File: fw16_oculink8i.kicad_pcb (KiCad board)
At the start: 4 copper layers, 118.7 x 72.5 mm, 24 parts, among them J1 FXBeam, J2 Fan0, J3 Fan1, J4 173162-0131, U1 BR24G32FVT-3GE2

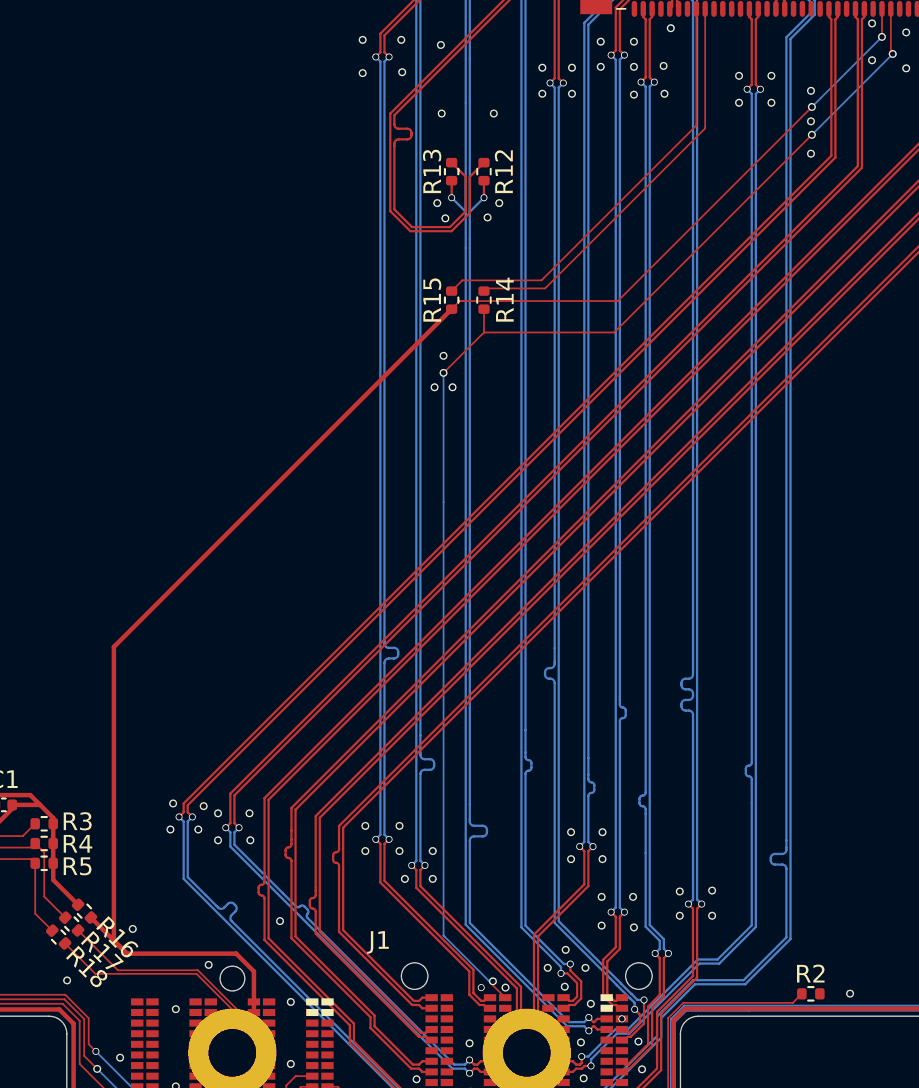
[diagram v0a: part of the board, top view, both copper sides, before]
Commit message: Add R0 resistor to CPRSNT oculink pin
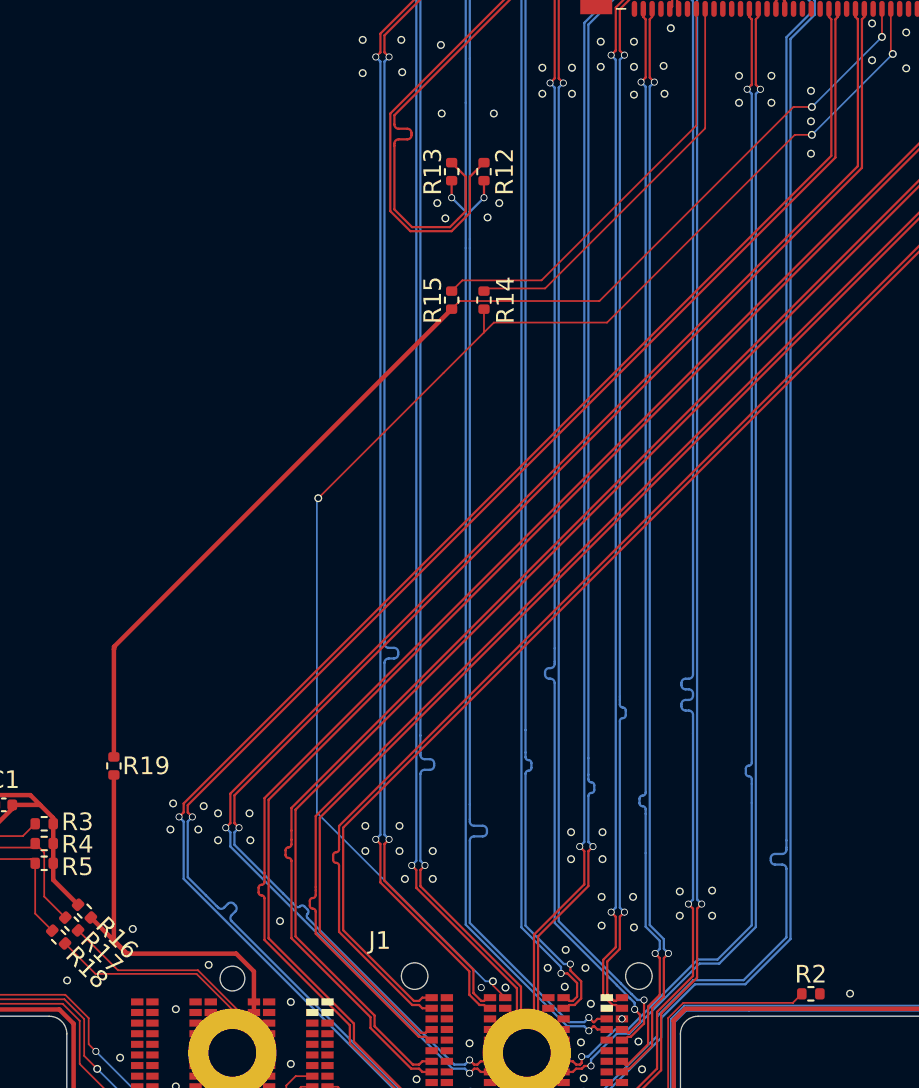
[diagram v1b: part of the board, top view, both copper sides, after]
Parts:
- added R19: 0R, Resistor_SMD:R_0402_1005Metric, F.Cu at (92.9, 75.0)
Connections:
- J4 pad B12: 3V3_ALW -> /CPRSNTA
- R15 pad 2: 3V3_ALW -> /CPRSNTA
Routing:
- net 3V3_ALW: track 89.8 -> 23.2 mm, vias 2 -> 0
- net /CPRSNTA: track 0.00 -> 65.5 mm, vias 0 -> 2
- net /PERSTA: track 73.7 -> 79.7 mm
- net GND: vias 137 -> 134

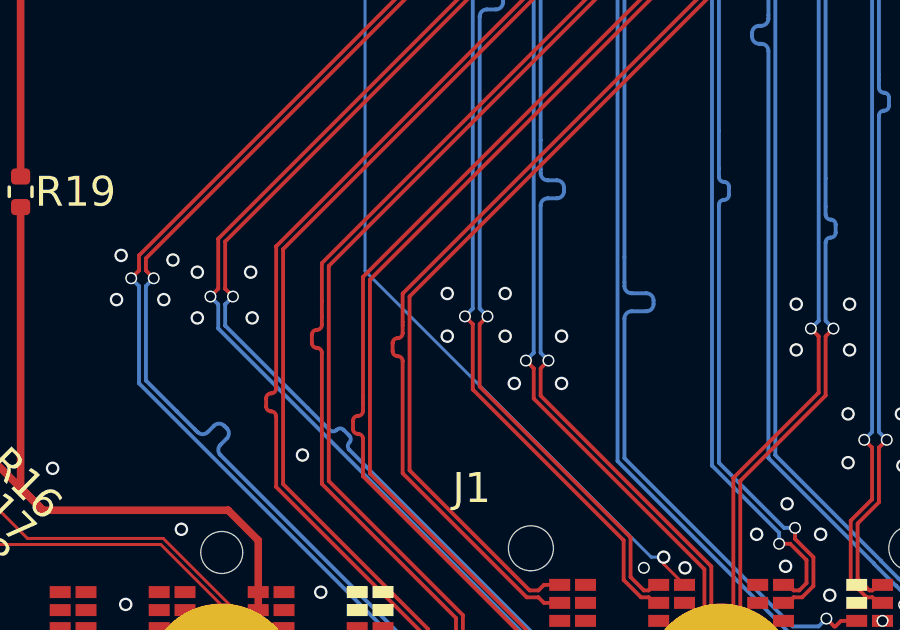
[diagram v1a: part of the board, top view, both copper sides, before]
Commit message: Remove unnecessary resistors from BOM
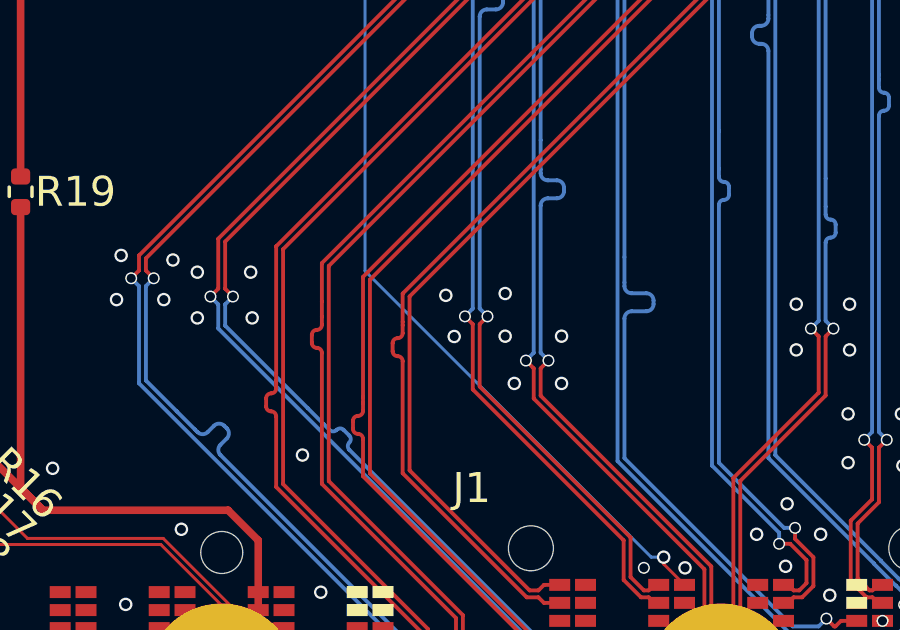
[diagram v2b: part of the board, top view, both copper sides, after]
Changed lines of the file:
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@@
 	)
 	(via
-		(at 107.083767 79.821767)
+		(at 107.315 79.8322)
 		(size 0.45)
 		(drill 0.3)
@@
 	)
 	(via
-		(at 107.083767 78.399367)
-		(size 0.45)
-		(drill 0.3)
+		(at 107.0356 78.4606)
+		(size 0.45)
+		(drill 0.3)

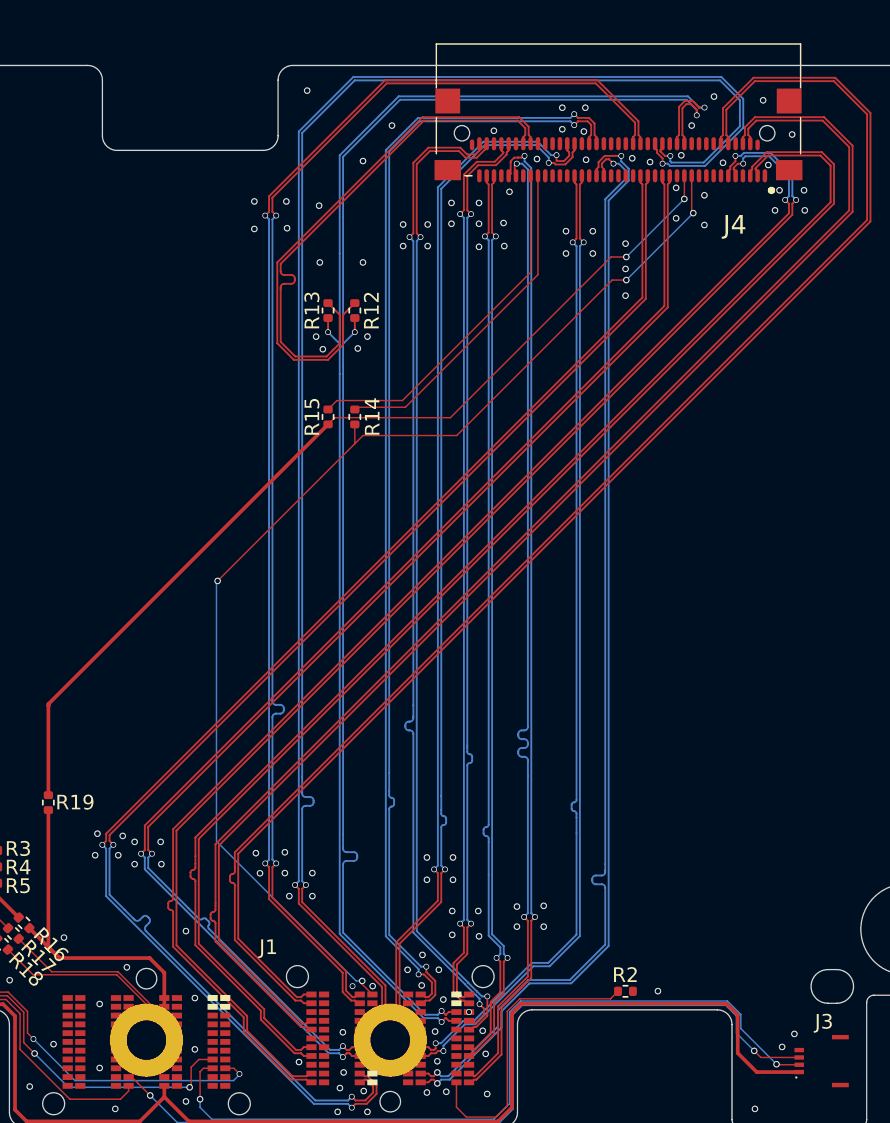
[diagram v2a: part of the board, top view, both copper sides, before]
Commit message: Create separate nano-pitch footprint with JLC DRC rules
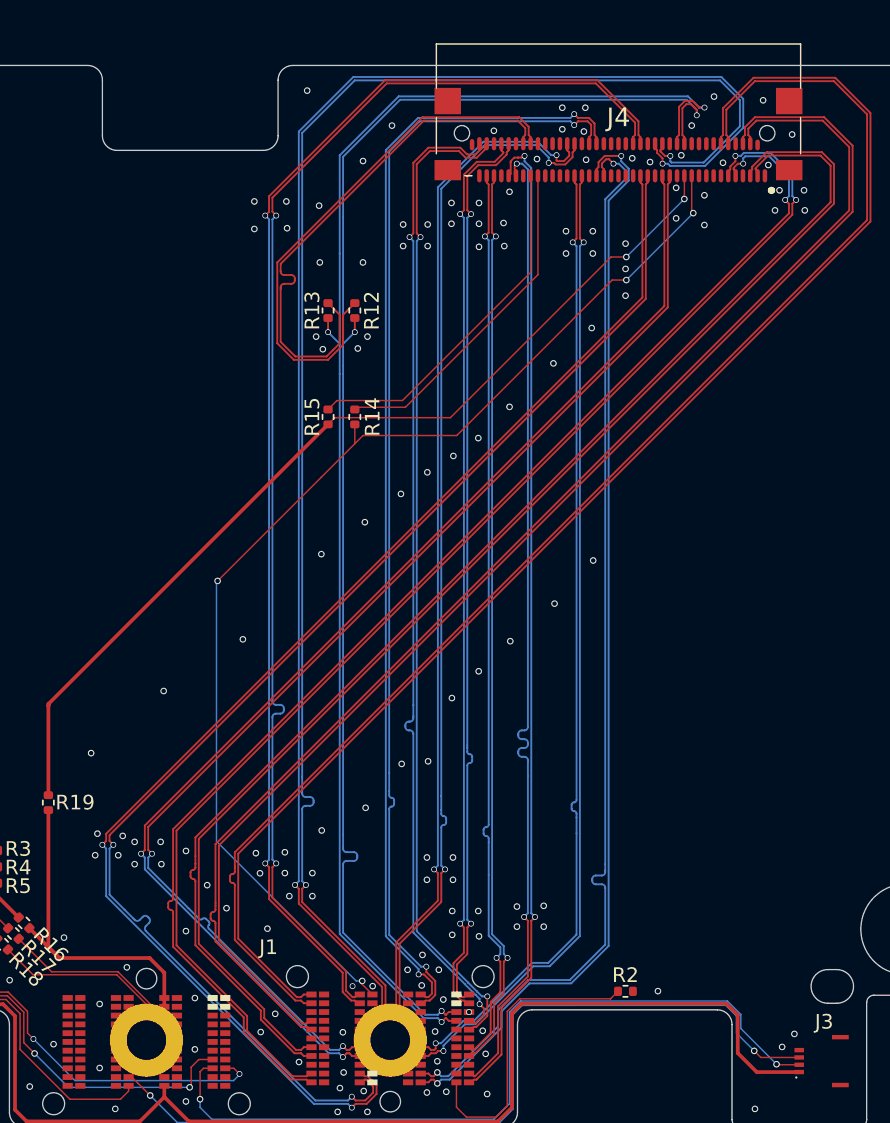
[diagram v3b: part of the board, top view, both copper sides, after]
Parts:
- J4: footprint Nano_Pitch:Nano-Pitch-173162-0131 -> Nano_Pitch:Nano-Pitch-173162-0131_JLC-DRC
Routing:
- net GND: vias 134 -> 161
